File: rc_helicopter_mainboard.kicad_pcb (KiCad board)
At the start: 2 copper layers, 0 parts

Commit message: Use single connector for I/O
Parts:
- added REF**: MountingHole_3mm_Pad_Via, MountingHole:MountingHole_3mm_Pad_Via, F.Cu at (170.0, 119.0)
- added REF**: MountingHole_3mm_Pad_Via, MountingHole:MountingHole_3mm_Pad_Via, F.Cu at (125.0, 119.0)
- added REF**: MountingHole_3mm_Pad_Via, MountingHole:MountingHole_3mm_Pad_Via, F.Cu at (125.0, 74.0)
- added REF**: MountingHole_3mm_Pad_Via, MountingHole:MountingHole_3mm_Pad_Via, F.Cu at (170.0, 74.0)
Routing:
- added copper zone on B.Cu, net +3.3V
- added copper zone on F.Cu, net GND
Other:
- board outline added: 55 x 55 mm

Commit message: Arrange footprints
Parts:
- added C1: 22pF, Capacitor_SMD:C_0603_1608Metric, F.Cu at (138.5, 103.5)
- added C10: 4.7μF, Capacitor_SMD:CP_Elec_6.3x5.4, F.Cu at (139.9, 91.8)
- added C11: 10μF, Capacitor_SMD:CP_Elec_6.3x5.4, F.Cu at (128.8, 102.7)
- added C12: 10μF, Capacitor_Tantalum_SMD:CP_EIA-3216-10_Kemet-I, F.Cu at (131.8, 97.2)
- added C13: 100nF, Capacitor_SMD:C_0603_1608Metric, F.Cu at (125.0, 111.6)
- added C14: 100nF, Capacitor_SMD:C_0603_1608Metric, F.Cu at (125.0, 108.3)
- added C15: 10nF, Capacitor_SMD:C_0603_1608Metric, F.Cu at (139.1, 83.0)
- added C16: 10μF, Capacitor_Tantalum_SMD:CP_EIA-3216-10_Kemet-I, F.Cu at (156.0, 118.8)
- added C17: 100nF, Capacitor_SMD:C_0603_1608Metric, F.Cu at (145.0, 99.8)
- added C18: 100nF, Capacitor_SMD:C_0603_1608Metric, F.Cu at (150.0, 97.1)
- added C19: 100nF, Capacitor_SMD:C_0603_1608Metric, F.Cu at (154.6, 98.8)
- added C2: 22pF, Capacitor_SMD:C_0603_1608Metric, F.Cu at (138.5, 109.5)
- added C20: 100nF, Capacitor_SMD:C_0603_1608Metric, F.Cu at (148.1, 99.8)
- added C21: 4.7μF, Capacitor_Tantalum_SMD:CP_EIA-3216-10_Kemet-I, F.Cu at (162.0, 87.5)
- added C3: 100nF, Capacitor_SMD:C_0603_1608Metric, F.Cu at (157.3, 113.0)
- added C4: 100nF, Capacitor_SMD:C_0603_1608Metric, F.Cu at (138.5, 111.2)
- added C5: 100nF, Capacitor_SMD:C_0603_1608Metric, F.Cu at (144.3, 115.0)
- added C6: 100nF, Capacitor_SMD:C_0603_1608Metric, F.Cu at (149.7, 115.0)
- added C7: 100nF, Capacitor_SMD:C_0603_1608Metric, F.Cu at (154.6, 104.8)
- added C8: 100nF, Capacitor_SMD:C_0603_1608Metric, F.Cu at (141.9, 99.8)
- added C9: 10nF, Capacitor_SMD:C_0603_1608Metric, F.Cu at (128.3, 91.7)
- added D1: SK36A, Diode_SMD:D_SMA, F.Cu at (125.5, 90.5)
- added D2: Blue, LED_SMD:LED_0603_1608Metric, F.Cu at (154.9, 84.6)
- added D3: Blue, LED_SMD:LED_0603_1608Metric, F.Cu at (152.9, 84.6)
- added D4: Blue, LED_SMD:LED_0603_1608Metric, F.Cu at (150.9, 84.6)
- added D5: Blue, LED_SMD:LED_0603_1608Metric, F.Cu at (148.9, 84.6)
- added D6: Blue, LED_SMD:LED_0603_1608Metric, F.Cu at (146.9, 84.6)
- added F1: 1A, Fuse:Fuse_1210_3225Metric, F.Cu at (132.2, 83.6)
- added G***: LOGO, Local_Library:Kiwi, F.Cu at (135.0, 116.7)
- added J1: Battery Pack, Connector_Molex:Molex_KK-254_AE-6410-02A_1x02_P2.54mm_Vertical, F.Cu at (126.0, 84.9)
- added J2: SWD, Connector_PinHeader_2.54mm:PinHeader_2x03_P2.54mm_Vertical, F.Cu at (158.3, 104.4)
- added J3: Main Connector, Connector_PinHeader_2.54mm:PinHeader_2x10_P2.54mm_Horizontal, F.Cu at (135.6, 79.1)
- added J4: Micro_SD_Card, Local_Library:112K-TAA0-RA1, F.Cu at (161.2, 94.4)
- added JP1: SolderJumper_3_Open, Jumper:SolderJumper-3_P1.3mm_Open_RoundedPad1.0x1.5mm_NumberLabels, F.Cu at (161.8, 77.0)
- added L1: 2.2μH, Inductor_SMD:L_Bourns-SRN4018, F.Cu at (126.3, 96.7)
- added R1: 10kΩ, Resistor_SMD:R_0603_1608Metric, F.Cu at (140.1, 101.7)
- added R10: 33kΩ, Resistor_SMD:R_0603_1608Metric, F.Cu at (137.5, 83.0)
- added R11: 140Ω, Resistor_SMD:R_0603_1608Metric, F.Cu at (154.9, 88.3)
- added R12: 140Ω, Resistor_SMD:R_0603_1608Metric, F.Cu at (152.9, 88.3)
- added R13: 140Ω, Resistor_SMD:R_0603_1608Metric, F.Cu at (150.9, 88.3)
- added R14: 140Ω, Resistor_SMD:R_0603_1608Metric, F.Cu at (148.9, 88.3)
- added R15: 140Ω, Resistor_SMD:R_0603_1608Metric, F.Cu at (146.9, 88.3)
- added R2: 10kΩ, Resistor_SMD:R_0603_1608Metric, F.Cu at (159.6, 113.0)
- added R3: 330Ω, Resistor_SMD:R_0603_1608Metric, F.Cu at (161.9, 113.0)
- added R4: 4.7kΩ, Resistor_SMD:R_0603_1608Metric, F.Cu at (162.0, 73.8)
- added R5: 4.7kΩ, Resistor_SMD:R_0603_1608Metric, F.Cu at (162.0, 80.2)
- added R6: 10kΩ, Resistor_SMD:R_0603_1608Metric, F.Cu at (131.1, 88.8)
- added R7: 39kΩ, Resistor_SMD:R_0603_1608Metric, F.Cu at (131.0, 94.8)
- added R8: 7.5kΩ, Resistor_SMD:R_0603_1608Metric, F.Cu at (133.4, 90.6)
- added R9: 100kΩ, Resistor_SMD:R_0603_1608Metric, F.Cu at (135.8, 83.0)
- added SW1: Tactswitch, Button_Switch_SMD:SW_SPST_PTS645, F.Cu at (166.5, 106.9)
- added U1: STM32L4P5RET6, Package_QFP:LQFP-64_10x10mm_P0.5mm, F.Cu at (147.0, 107.4)
- added U2: AOZ1280CI, Package_TO_SOT_SMD:SOT-23-6, F.Cu at (130.9, 91.7)
- added U3: LM1117-3.3, Package_TO_SOT_SMD:SOT-223-3_TabPin2, F.Cu at (130.3, 110.0)
- added U4: LM321, Package_TO_SOT_SMD:SOT-23-5, F.Cu at (141.7, 83.6)
- added U5: NRF24L01_Breakout, RF_Module:nRF24L01_Breakout, F.Cu at (152.4, 117.5)
- added U6: MPU-9250, Sensor_Motion:InvenSense_QFN-24_3x3mm_P0.4mm, F.Cu at (147.0, 97.0)
- added U7: BMP280, Package_LGA:Bosch_LGA-8_2x2.5mm_P0.65mm_ClockwisePinNumbering, F.Cu at (154.6, 96.4)
- added Y1: 16MHz, Crystal:Crystal_SMD_3225-4Pin_3.2x2.5mm, F.Cu at (138.4, 106.5)
- moved REF** 4.24 mm to (167.0, 77.0)
- moved REF** 3.61 mm to (167.0, 117.0)
- moved REF** 3.61 mm to (127.0, 77.0)
- moved REF** 2.83 mm to (127.0, 117.0)
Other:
- board size 55 x 55 mm -> 50 x 50 mm
- board text added: "DEBUG"
- board text added: "Mainboard"
- board text added: "RESET"
- board text added: "Rev: ${REVISION}"
- board text added: "SWD"

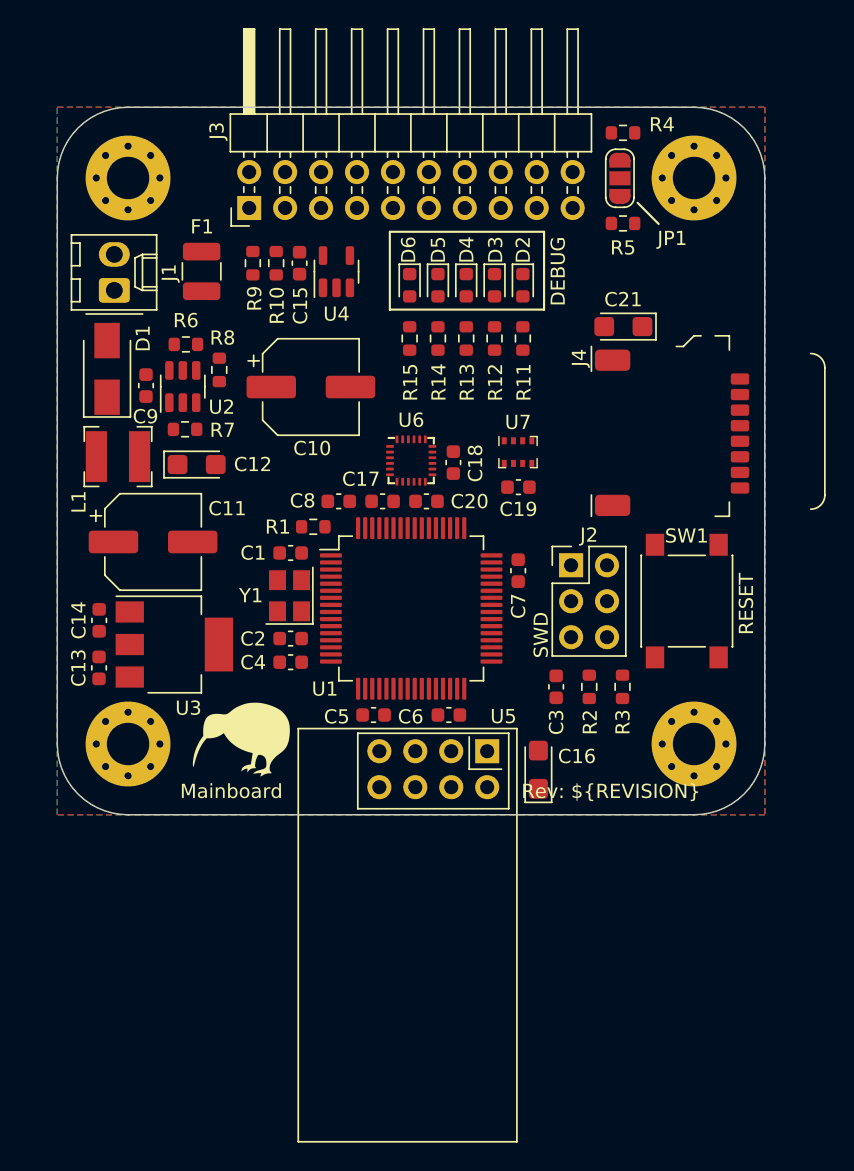
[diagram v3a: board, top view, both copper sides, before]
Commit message: Rearrange footprints
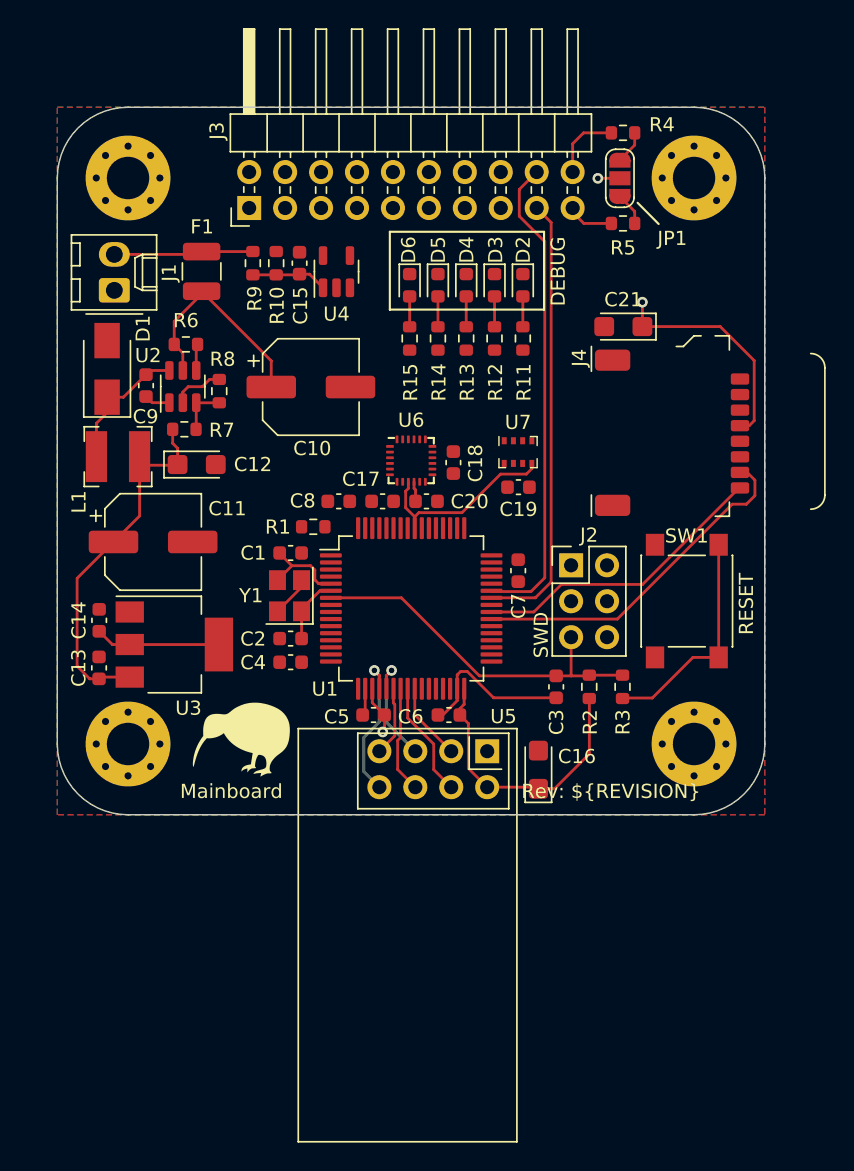
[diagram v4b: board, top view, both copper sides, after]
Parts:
- moved R8 1.50 mm to (133.4, 92.1)
- moved R7 0.05 mm to (131.0, 94.8)
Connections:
- J2 pad 6: /SWO -> unconnected-(J2-Pad6)
- U1 pad 10: /MISO -> unconnected-(U1-Pad10)
- U1 pad 11: /BMP_SS -> unconnected-(U1-Pad11)
- U1 pad 14: /UART_TX -> /ROT_SERVO2
- U1 pad 15: /UART_RX -> /ROT_SERVO1
- U1 pad 16: unconnected-(U1-Pad16) -> /TAIL_ROT_ESC
- U1 pad 17: /V_BATT -> /MAIN_ROT_ESC
- U1 pad 2: /LED1 -> unconnected-(U1-Pad2)
- U1 pad 20: /NRF_CSN -> /NRF_IRQ
- U1 pad 24: /MPU_SS -> /NRF_CSN
- U1 pad 25: /MPU_INT -> /NRF_CE
- U1 pad 26: /NRF_CE -> unconnected-(U1-Pad26)
- U1 pad 27: /LED5 -> unconnected-(U1-Pad27)
- U1 pad 29: /CLK -> unconnected-(U1-Pad29)
- U1 pad 3: /LED2 -> unconnected-(U1-Pad3)
- U1 pad 34: /I2C_SCL -> /LED5
- U1 pad 35: /I2C_SDA -> /LED4
- U1 pad 36: unconnected-(U1-Pad36) -> /LED3
- U1 pad 37: /MPU_FSYNC -> /LED2
- U1 pad 38: unconnected-(U1-Pad38) -> /LED1
- U1 pad 4: /LED3 -> unconnected-(U1-Pad4)
- U1 pad 41: /NRF_IRQ -> unconnected-(U1-Pad41)
- U1 pad 42: unconnected-(U1-Pad42) -> /UART_TX
- U1 pad 43: unconnected-(U1-Pad43) -> /UART_RX
- U1 pad 44: unconnected-(U1-Pad44) -> /BMP_SS
- U1 pad 45: unconnected-(U1-Pad45) -> /MPU_INT
- U1 pad 50: unconnected-(U1-Pad50) -> /MPU_FSYNC
- U1 pad 55: /SWO -> /SCK
- U1 pad 56: /ROT_SERVO1 -> /MISO
- U1 pad 57: /ROT_SERVO2 -> /MOSI
- U1 pad 58: /MAIN_ROT_ESC -> /I2C_SCL
- U1 pad 59: /TAIL_ROT_ESC -> /I2C_SDA
- U1 pad 61: unconnected-(U1-Pad61) -> /MPU_SS
- U1 pad 8: /LED4 -> /V_BATT
- U1 pad 9: /MOSI -> unconnected-(U1-Pad9)
- U6 pad 23: /CLK -> /SCK
- U7 pad 4: /CLK -> /SCK
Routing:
- net +3.3V: track 0.00 -> 50.0 mm, vias 0 -> 3
- net /UART_RX: track 0.00 -> 34.1 mm
- net /UART_TX: track 0.00 -> 31.5 mm
- net +5V: track 0.00 -> 26.4 mm
- net /NRST: track 0.00 -> 25.7 mm
- net /SDMMC_D0: track 0.00 -> 24.6 mm
- net /SDMMC_D1: track 0.00 -> 21.2 mm
- net GND: track 0.00 -> 20.0 mm
- net Net-(R3-Pad2): track 0.00 -> 16.0 mm
- net Net-(C10-Pad1): track 0.00 -> 15.5 mm
- net /MISO: track 0.00 -> 13.7 mm
- net /NRF_IRQ: track 0.00 -> 10.7 mm, vias 0 -> 1
- net +BATT: track 0.00 -> 9.87 mm
- net Net-(C9-Pad2): track 0.00 -> 9.69 mm
- net /NRF_CSN: track 0.00 -> 8.23 mm
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
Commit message: Route PCB tracks
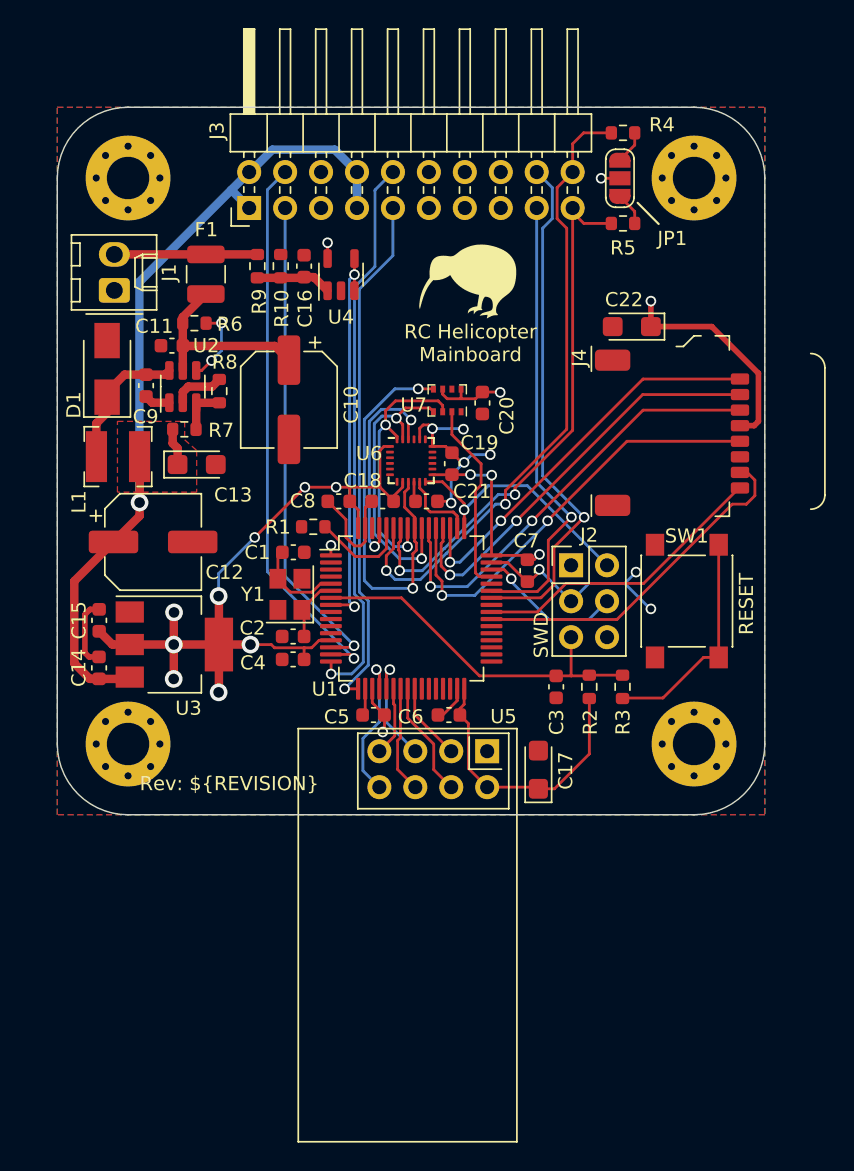
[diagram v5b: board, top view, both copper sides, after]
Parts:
- removed D2, D3, D4, D5, D6: Blue, LED_SMD:LED_0603_1608Metric
- removed R11, R12, R13, R14, R15: 140Ω, Resistor_SMD:R_0603_1608Metric
- added C11: 100nF, Capacitor_SMD:C_0603_1608Metric, F.Cu at (130.1, 88.8)
- moved G*** 36.1 mm to (151.0, 84.3)
- moved C20 6.47 mm to (152.0, 92.9), turned to -90 degrees
- moved U7 6.19 mm to (149.6, 92.7), turned to 180 degrees
- moved C10 1.79 mm to (138.4, 92.7), turned to -90 degrees
- moved R6 1.62 mm to (131.7, 87.3)
- moved C7 0.65 mm to (155.2, 104.8)
- moved C22 0.60 mm to (162.6, 87.5)
- moved U4 0.38 mm to (142.1, 83.8)
- moved C16 0.38 mm to (139.4, 83.2)
- moved R10 0.38 mm to (137.8, 83.2)
- moved R9 0.38 mm to (136.1, 83.2)
- moved F1 0.36 mm to (132.5, 83.8)
- moved C4 0.27 mm to (138.7, 111.0)
- moved C2 0.23 mm to (138.7, 109.4)
- moved C1 0.20 mm to (138.7, 103.5)
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- renumbered C11 to C12, C12 to C13, C13 to C14, C14 to C15, C15 to C16, C16 to C17, C17 to C18, C18 to C19, C19 to C20, C20 to C21, C21 to C22
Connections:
- J2 pad 2: /SWCLK -> /MPU_INT (SWCLK)
- J3 pad 17: /UART_TX -> /UART_RX
- J3 pad 18: /UART_RX -> /UART_TX
- U1 pad 14: /ROT_SERVO2 -> /ROT_SERVO1
- U1 pad 15: /ROT_SERVO1 -> /ROT_SERVO2
- U1 pad 34: /LED5 -> unconnected-(U1-Pad34)
- U1 pad 35: /LED4 -> unconnected-(U1-Pad35)
- U1 pad 36: /LED3 -> unconnected-(U1-Pad36)
- U1 pad 37: /LED2 -> unconnected-(U1-Pad37)
- U1 pad 38: /LED1 -> unconnected-(U1-Pad38)
- U1 pad 44: /BMP_SS -> unconnected-(U1-Pad44)
- U1 pad 45: /MPU_INT -> /BMP_SS
- U1 pad 49: /SWCLK -> /MPU_INT (SWCLK)
- U6 pad 12: /MPU_INT -> /MPU_INT (SWCLK)
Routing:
- net +3.3V: track 50.0 -> 115.9 mm, vias 3 -> 18
- net /I2C_SDA: track 5.05 -> 45.2 mm, vias 0 -> 2
- net /TAIL_ROT_ESC: track 0.00 -> 39.5 mm, vias 0 -> 1
- net /ROT_SERVO2: track 0.00 -> 39.2 mm, vias 0 -> 1
- net +5V: track 26.4 -> 63.4 mm, vias 0 -> 1
- net /MAIN_ROT_ESC: track 0.00 -> 36.9 mm, vias 0 -> 1
- net /I2C_SCL: track 3.36 -> 38.8 mm, vias 0 -> 2
- net /ROT_SERVO1: track 0.00 -> 34.6 mm, vias 0 -> 1
- net /SDMMC_CMD: track 0.00 -> 31.2 mm, vias 0 -> 2
- net GND: track 20.0 -> 51.1 mm, vias 0 -> 8
- net /SDMMC_CLK: track 0.00 -> 30.6 mm, vias 0 -> 2
- net /SDMMC_D3: track 0.00 -> 29.4 mm, vias 0 -> 2
- net /SDMMC_D2: track 0.00 -> 28.2 mm, vias 0 -> 2
- net /V_BATT: track 0.00 -> 27.8 mm, vias 0 -> 2
- net /SCK: track 0.00 -> 20.6 mm, vias 0 -> 2
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- added copper zone on F.Cu, net +5V
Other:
- board text added: "RC Helicopter Mainboard"
- board text removed: "DEBUG"
- board text removed: "Mainboard"
